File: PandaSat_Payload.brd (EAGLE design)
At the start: 93.9 x 90.2 mm, 16 parts, among them J1 U.FL, J5 U.FL, J6 FEMALE 2x3, U1 CH340G, U12 EP2W+, U14 S1216V8, Y1 12MHz

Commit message: Adding last version of Panda_Payload PCB
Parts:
- removed X3: (no value), con-berg:PN87520
- added J2: (no value), SparkFun-Connectors:1X04
- moved J5 90.6 mm to (10.9, 87.0), flipped to the top, turned to 270 degrees
- moved U12 60.1 mm to (17.8, 86.0), flipped to the top
- moved U1 50.3 mm to (24.0, 32.5), flipped to the top
- moved Y1 46.8 mm to (21.0, 42.9), flipped to the top, turned to 180 degrees
- moved J1 45.7 mm to (24.6, 87.0), flipped to the top, turned to 270 degrees
- moved C2 40.6 mm to (24.7, 43.0), flipped to the top, turned to 90 degrees
- moved C7 40.6 mm to (24.7, 39.4), flipped to the top, turned to 90 degrees
- moved C8 36.8 mm to (17.1, 41.1), flipped to the top, turned to 90 degrees
- moved U14 33.2 mm to (22.8, 76.0), flipped to the top, turned to 90 degrees
- moved J6 29.1 mm to (40.2, 75.0), turned to 270 degrees
- moved C1 28.0 mm to (24.7, 46.6), flipped to the top, turned to 270 degrees
- moved X1 3.73 mm to (58.3, 76.9)
- moved PCB1 1.19 mm to (5.52, 7.77)
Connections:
- net ENABLE renamed ENABLE1
- removed net N$10: X3.3
- removed net N$8: U1.6, X3.2
- removed net N$9: U1.5, X3.1
- removed net SHLD: X3.4
- new net ENABLE2: J6.5
- new net GPS_CLK: PCB1.P$18, U14.3
- new net UD+: J2.2, U1.5
- new net UD-: J2.3, U1.6
- net GND: now also J2.1
- net VCC3.3: no longer J6.5
- net VCC5: now also J2.4
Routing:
- net GND: track 91.4 -> 284.5 mm, vias 0 -> 1
- net VCC5: track 0.00 -> 116.4 mm
- net U.FL1: track 93.3 -> 5.09 mm
- net UD-: track 0.00 -> 85.8 mm, vias 0 -> 1
- net UD+: track 0.00 -> 78.4 mm
- net UART2_TX: track 0.00 -> 35.4 mm, vias 0 -> 1
- net UART2_RX: track 0.00 -> 35.0 mm, vias 0 -> 1
- net RXI: track 0.00 -> 34.7 mm, vias 0 -> 2
- net TXO: track 0.00 -> 34.7 mm, vias 0 -> 2
- net RF_IN: track 33.7 -> 1.75 mm
- net GPS_CLK: track 0.00 -> 31.0 mm
- net GPS_RSTN: track 0.00 -> 29.1 mm
- net VCC: track 0.00 -> 28.1 mm
- net U.FL2: track 32.6 -> 5.07 mm
- net VCC3.3: track 0.00 -> 24.3 mm, vias 0 -> 2
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
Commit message: Added Last version of PandaSat_Payload sch/board
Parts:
- added J3: (no value), SparkFun-Connectors:1X04
- added J4: FEMALE 2x3, SparkFun-Connectors:2X3
- moved C8 18.0 mm to (29.3, 27.8), turned to 0 degrees
- moved X1 7.80 mm to (50.7, 78.7), turned to 90 degrees
- moved C2 6.44 mm to (20.9, 37.8), turned to 180 degrees
- moved C1 5.60 mm to (24.0, 41.0), turned to 90 degrees
- moved Y1 1.96 mm to (21.0, 41.0)
- moved C7 1.69 mm to (24.0, 37.8), turned to 180 degrees
- moved J1 0.69 mm to (25.0, 86.5), turned to 180 degrees
- moved J5 0.69 mm to (10.6, 86.4), turned to 0 degrees
- moved J6 0.54 mm to (39.7, 75.0)
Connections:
- removed net ENABLE2: J6.5
- removed net GPS_ANTENNA_1: J1.1, J1.2
- removed net GPS_ANTENNA_2: J5.1, J5.2
- removed net VCC: C8.1, U1.16
- new net D2+: J3.2, J4.5
- new net D2-: J3.3, J4.3
- net ENABLE1: now also J6.2; no longer J6.6
- net GND: now also J1.1, J1.2, J3.1, J4.1, J4.2, J4.4, J5.1, J5.2, J6.3; no longer J6.1
- net UART2_RX: now also J6.6; no longer J6.2
- net VCC5: now also C8.1, J3.4, J4.6, J6.1, U1.16; no longer J6.3
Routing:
- net GND: track 284.5 -> 74.9 mm, vias 1 -> 18
- net VCC5: track 116.4 -> 202.1 mm
- net D2+: track 0.00 -> 81.7 mm, vias 0 -> 1
- net D2-: track 0.00 -> 79.7 mm
- net VCC: track 28.1 -> 0.00 mm
- net ENABLE1: track 21.2 -> 30.1 mm, vias 1 -> 0
- net N$2: track 13.5 -> 5.09 mm
- net GPS_CLK: track 31.0 -> 22.7 mm
- net UART2_RX: track 35.0 -> 28.2 mm
- net N$5: track 15.3 -> 8.95 mm
- net UART2_TX: track 35.4 -> 31.6 mm
- net GPS_ANTENNA_2: track 2.75 -> 0.00 mm
- net GPS_ANTENNA_1: track 2.75 -> 0.00 mm
- net UD-: track 85.8 -> 83.5 mm
- net UD+: track 78.4 -> 80.1 mm
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- added copper zone on layer 1, net GND
- added copper zone on layer 16, net GND
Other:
- outline, holes or cut-outs redrawn

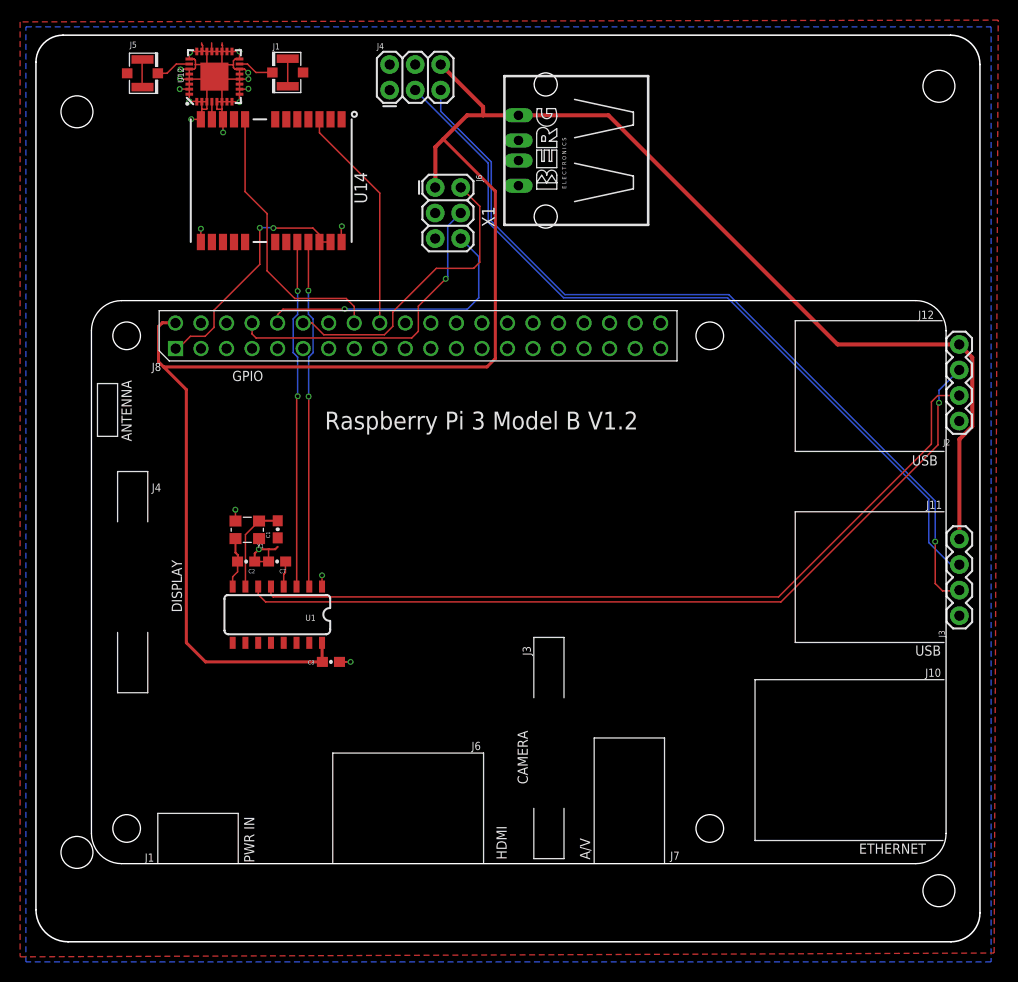
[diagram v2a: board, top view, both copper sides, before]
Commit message: Added changes to the EAGLE files on the board
changed position of the SDR USB socket
changed the position of the USB 4 pins connector (closer to the Pi holes)
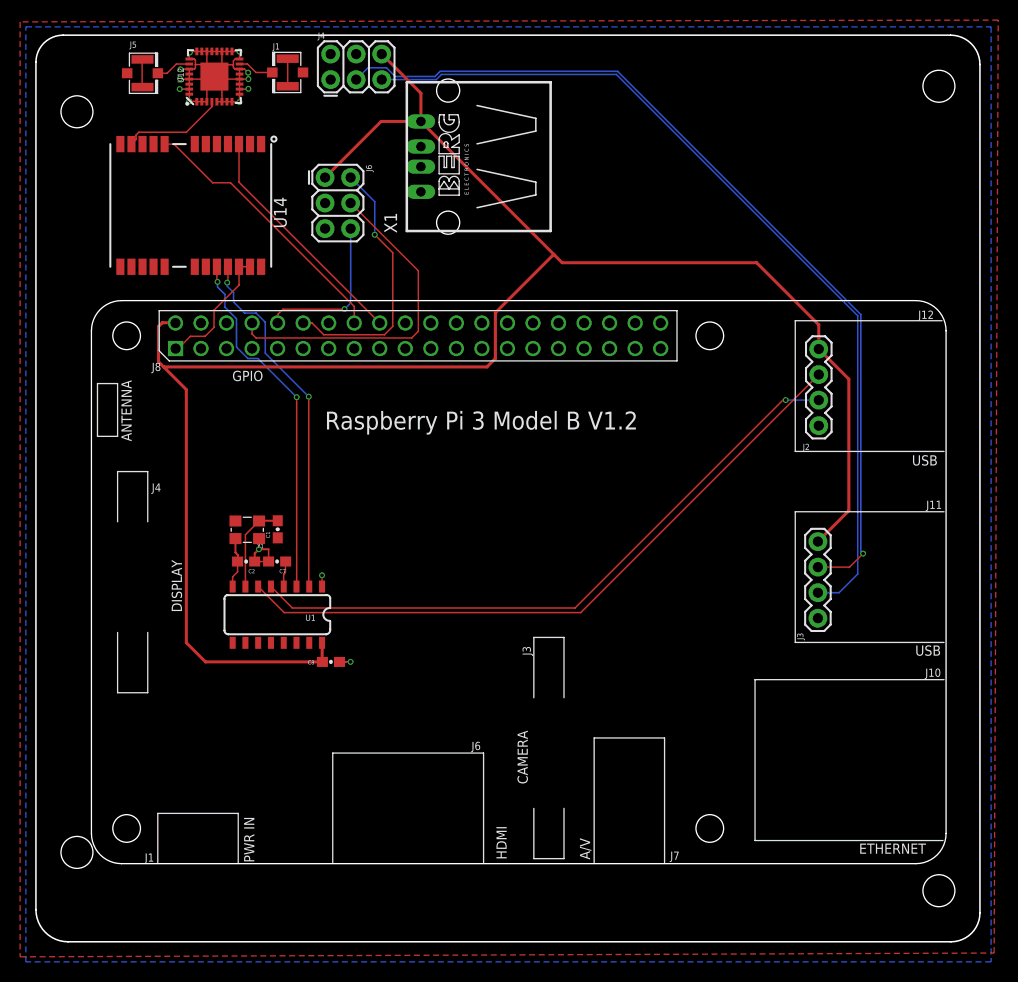
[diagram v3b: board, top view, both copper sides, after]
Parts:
- removed FRAME1, FRAME2: FRAME-LETTERNO_PACKAGE, SparkFun-Aesthetics:DUMMY
- moved J3 14.1 mm to (77.8, 32.2)
- moved J2 14.0 mm to (77.9, 51.3)
- moved J6 11.0 mm to (28.8, 76.0)
- moved X1 9.72 mm to (41.0, 78.1)
- moved U14 8.37 mm to (14.8, 73.5)
- moved J4 5.96 mm to (29.3, 85.8)
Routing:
- net UD-: track 83.5 -> 66.6 mm, vias 1 -> 0
- net UD+: track 80.1 -> 63.9 mm, vias 0 -> 1
- net GND: track 74.9 -> 58.7 mm, vias 18 -> 13
- net VCC5: track 202.1 -> 189.0 mm
- net UART2_RX: track 28.2 -> 16.0 mm
- net VCC3.3: track 24.5 -> 12.9 mm, vias 2 -> 0
- net D2-: track 79.7 -> 90.2 mm, vias 0 -> 1
- net RF_IN: track 1.75 -> 10.3 mm
- net D2+: track 81.7 -> 87.9 mm, vias 1 -> 0
- net ENABLE1: track 30.1 -> 26.3 mm, vias 0 -> 1
- net UART2_TX: track 31.6 -> 33.6 mm, vias 1 -> 0
- net TXO: track 34.7 -> 35.9 mm
- net RXI: track 34.7 -> 35.7 mm
- net GPS_CLK: track 22.7 -> 23.6 mm
- net GPS_RSTN: track 27.8 -> 27.2 mm

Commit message: Added last changes for new board
vias diameters
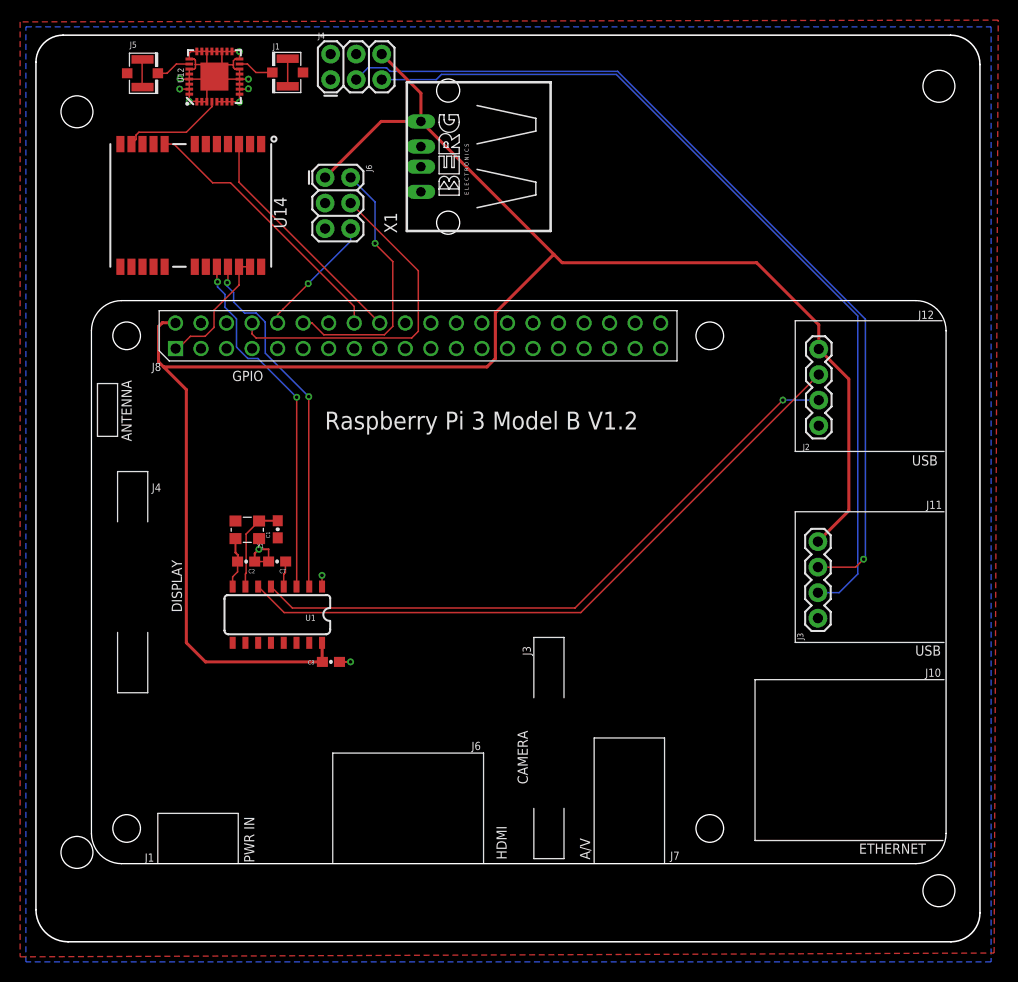
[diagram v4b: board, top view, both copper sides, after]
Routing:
- net GND: track 58.7 -> 54.0 mm, vias 13 -> 10
- net UART2_RX: track 16.0 -> 12.4 mm
